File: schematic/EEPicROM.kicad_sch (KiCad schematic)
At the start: 11 parts, among them Q1 IRF4905, U1 AT28piCo256_headers, U2 Pico, U3 TXS0108EPW, U4 TXS0108EPW, U5 TXS0108EPW

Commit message: Add README.md and change some things
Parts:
- added D1: LED, symbol Device:LED
- added R1: 560, symbol Device:R
- added SW1: SW_Push, symbol Switch:SW_Push
- R2: renamed from R5; value 1K -> 1k
- R3: renamed from R1; value 5K -> 5k
- R4: renamed from R2; value 5K -> 5k
- R5: renamed from R3; value 5K -> 5k
- R6: renamed from R4; value 5K -> 5k
- renumbered U2 to U1, U3 to U2, U4 to U3, U1 to U4
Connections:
- net +3V3: now also D1.2 (A)
- net +5V: now also R1.1
- net GND: now also U1.30 (RUN), D1.1 (K), SW1.2
- new net: R1.2, SW1.1
- no-connect marks 6 -> 5
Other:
- moved on the sheet: Q1, R2, R3, R4, R5, R6, U1, U2, U3, U4A, U4B, U5

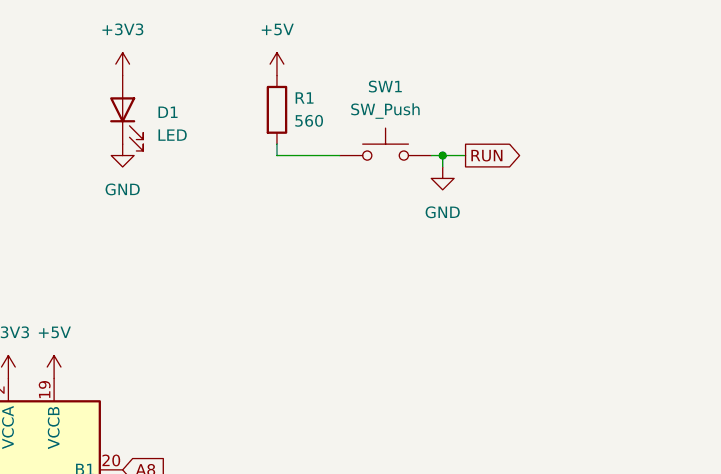
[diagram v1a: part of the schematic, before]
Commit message: Fix RUN button circuit in schematic
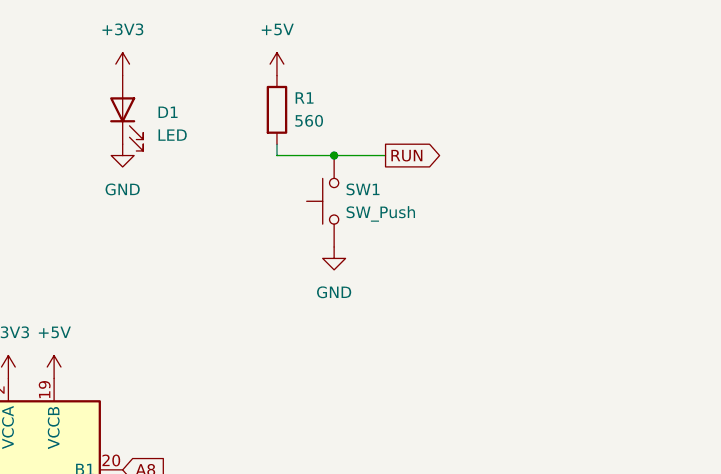
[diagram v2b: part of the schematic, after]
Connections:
- net GND: now also SW1.1; no longer SW1.2, U1.30 (RUN)
- net RUN: now reaches R1.2
- net RUN: now also SW1.2, U1.30 (RUN); no longer SW1.1
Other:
- moved on the sheet: SW1
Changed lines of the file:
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@@
     (title "EEPicROM")
     (date "2022-06-26")
-    (rev "6")
+    (rev "6.1")
     (company "lilakerl")
   )
@@
   (junction (at 156.845 109.855) (diameter 0) (color 0 0 0 0)
   )
+  (junction (at 226.695 44.45) (diameter 0) (color 0 0 0 0)
+  )
   (junction (at 156.845 84.455) (diameter 0) (color 0 0 0 0)
   )
@@
   )
   (junction (at 141.605 120.015) (diameter 0) (color 0 0 0 0)
-  )
-  (junction (at 238.76 44.45) (diameter 0) (color 0 0 0 0)
   )
   (junction (at 156.845 97.155) (diameter 0) (color 0 0 0 0)
@@
     (stroke (width 0) (type default) (color 0 0 0 0))
   )
-  (wire (pts (xy 220.345 44.45) (xy 227.33 44.45))
+  (wire (pts (xy 220.345 44.45) (xy 226.695 44.45))
     (stroke (width 0) (type default) (color 0 0 0 0))
   )
@@
     (stroke (width 0) (type default) (color 0 0 0 0))
   )
-  (wire (pts (xy 238.76 44.45) (xy 238.76 45.72))
-    (stroke (width 0) (type default) (color 0 0 0 0))
-  )
   (wire (pts (xy 236.855 130.175) (xy 236.855 131.445))
     (stroke (width 0) (type default) (color 0 0 0 0))
@@
     (stroke (width 0) (type default) (color 0 0 0 0))
   )
+  (wire (pts (xy 226.695 44.45) (xy 232.41 44.45))
+    (stroke (width 0) (type default) (color 0 0 0 0))
+  )
   (wire (pts (xy 182.88 81.915) (xy 175.895 81.915))
     (stroke (width 0) (type default) (color 0 0 0 0))
@@
     (stroke (width 0) (type default) (color 0 0 0 0))
   )
-  (wire (pts (xy 237.49 44.45) (xy 238.76 44.45))
-    (stroke (width 0) (type default) (color 0 0 0 0))
-  )
   (wire (pts (xy 182.88 79.375) (xy 177.165 79.375))
     (stroke (width 0) (type default) (color 0 0 0 0))
@@
     (stroke (width 0) (type default) (color 0 0 0 0))
   )
-  (wire (pts (xy 238.76 44.45) (xy 241.3 44.45))
-    (stroke (width 0) (type default) (color 0 0 0 0))
-  )
   (wire (pts (xy 172.085 89.535) (xy 172.085 102.235))
     (stroke (width 0) (type default) (color 0 0 0 0))
@@
     )
   )
-  (global_label "RUN" (shape output) (at 241.3 44.45 0) (fields_autoplaced)
-    (effects (font (size 1.27 1.27)) (justify left))
-    (property "Intersheet References" "${INTERSHEET_REFS}" (id 0) (at 247.6441 44.3706 0)
+  (global_label "RUN" (shape output) (at 232.41 44.45 0) (fields_autoplaced)
+    (effects (font (size 1.27 1.27)) (justify left))
+    (property "Intersheet References" "${INTERSHEET_REFS}" (id 0) (at 238.7541 44.3706 0)
       (effects (font (size 1.27 1.27)) (justify left) hide)
     )
@@
     (pin "9")
   )
-  (symbol (lib_id "power:GND") (at 238.76 45.72 0) (unit 1)
-    (in_bom yes) (on_board yes) (fields_autoplaced)
-    (property "Reference" "#PWR04" (id 0) (at 238.76 52.07 0)
-      (effects (font (size 1.27 1.27)) hide)
-    )
-    (property "Value" "GND" (id 1) (at 238.76 50.8 0))
-    (property "Footprint" "" (id 2) (at 238.76 45.72 0)
-      (effects (font (size 1.27 1.27)) hide)
-    )
-    (property "Datasheet" "" (id 3) (at 238.76 45.72 0)
+  (symbol (lib_id "power:GND") (at 226.695 54.61 0) (unit 1)
+    (in_bom yes) (on_board yes) (fields_autoplaced)
+    (property "Reference" "#PWR04" (id 0) (at 226.695 60.96 0)
+      (effects (font (size 1.27 1.27)) hide)
+    )
+    (property "Value" "GND" (id 1) (at 226.695 59.69 0))
+    (property "Footprint" "" (id 2) (at 226.695 54.61 0)
+      (effects (font (size 1.27 1.27)) hide)
+    )
+    (property "Datasheet" "" (id 3) (at 226.695 54.61 0)
       (effects (font (size 1.27 1.27)) hide)
     )
@@
     (pin "1")
   )
-  (symbol (lib_id "Switch:SW_Push") (at 232.41 44.45 0) (unit 1)
-    (in_bom yes) (on_board yes) (fields_autoplaced)
-    (property "Reference" "SW1" (id 0) (at 232.41 36.83 0))
-    (property "Value" "SW_Push" (id 1) (at 232.41 39.37 0))
-    (property "Footprint" "" (id 2) (at 232.41 39.37 0)
-      (effects (font (size 1.27 1.27)) hide)
-    )
-    (property "Datasheet" "~" (id 3) (at 232.41 39.37 0)
-      (effects (font (size 1.27 1.27)) hide)
-    )
+  (symbol (lib_id "Switch:SW_Push") (at 226.695 49.53 90) (unit 1)
+    (in_bom yes) (on_board yes) (fields_autoplaced)
+    (property "Reference" "SW1" (id 0) (at 227.965 48.2599 90)
+      (effects (font (size 1.27 1.27)) (justify right))
+    )
+    (property "Value" "SW_Push" (id 1) (at 227.965 50.7999 90)
+      (effects (font (size 1.27 1.27)) (justify right))
+    )
+    (property "Footprint" "" (id 2) (at 221.615 49.53 0)
+      (effects (font (size 1.27 1.27)) hide)
+    )
+    (property "Datasheet" "~" (id 3) (at 221.615 49.53 0)
+      (effects (font (size 1.27 1.27)) hide)
+    )
